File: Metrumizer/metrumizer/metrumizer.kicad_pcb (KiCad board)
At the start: 2 copper layers, 83 parts, among them J1 Conn_01x03, J2 USB_B_Micro, J3 Conn_01x04, J4 Conn_01x03, Q1 AO3401A, Q2 AO3401A, Q3 Si7232DN, U1 ATSAMD21G17A-M, U10 LM293, U2 CC1200, U3 W25Q128JVS, U4 ADXL375BCCZ-RL7, U5 MS5607-02BA, U6 MAX-M10S, U7 MCP130-315, U8 XC6206P332MR, Y1 X322516MLB4SI, Y2 YF4040M00033T8188097

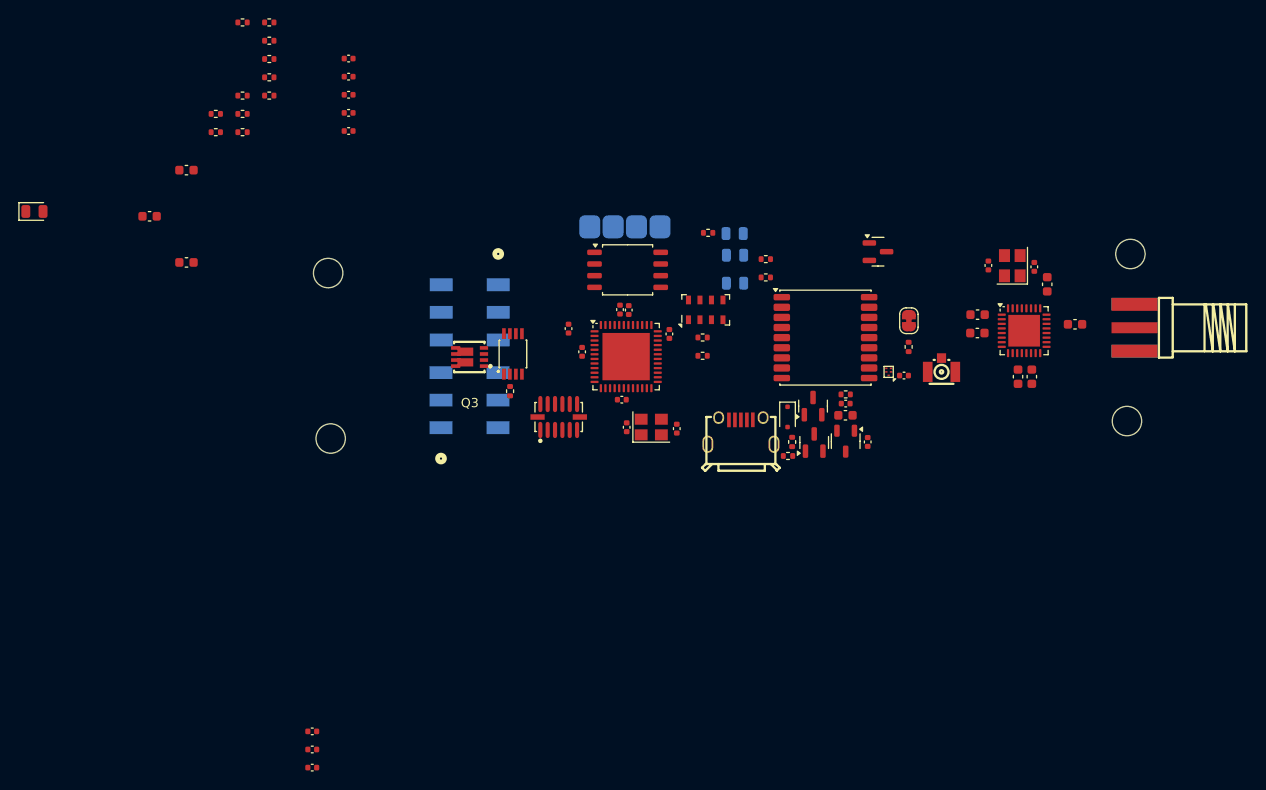
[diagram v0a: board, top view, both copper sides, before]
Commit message: dan f10, n511 module, board layout
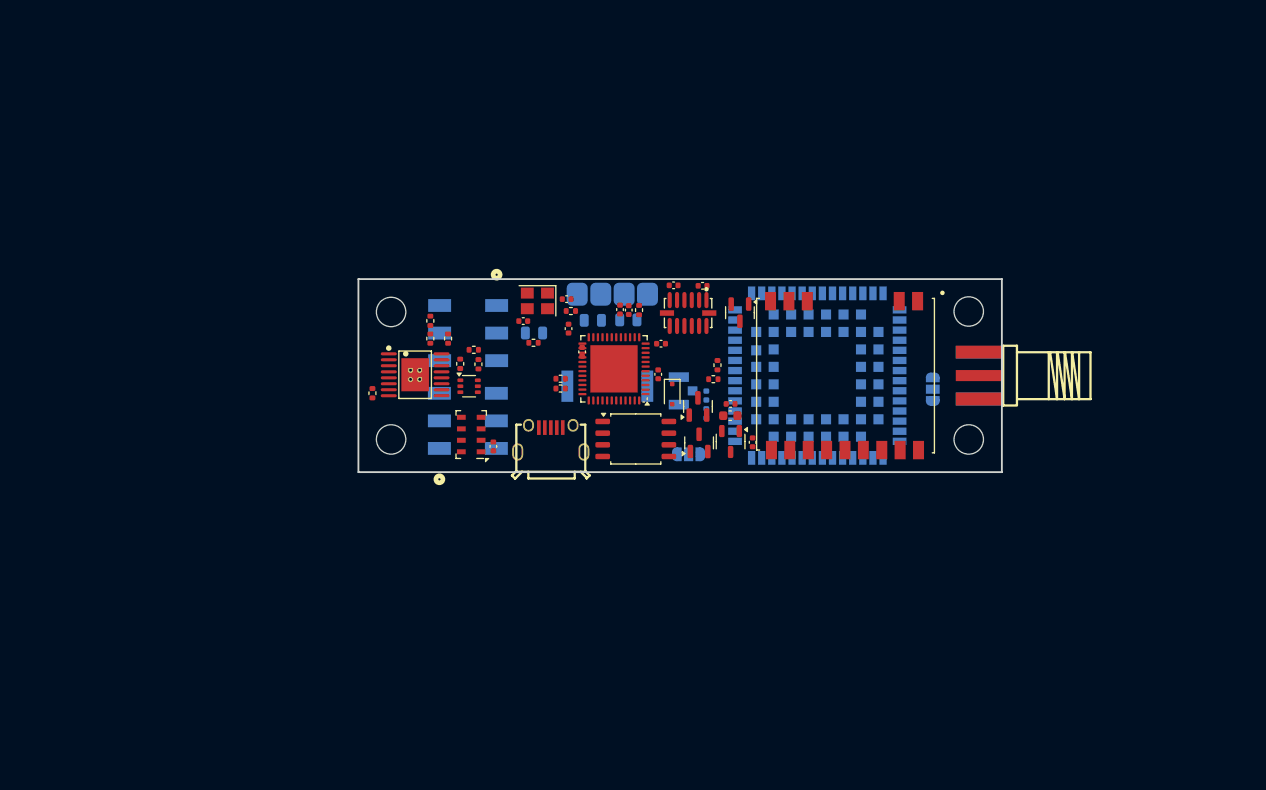
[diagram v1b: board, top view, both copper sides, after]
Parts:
- removed AE1: IPEX, .pretty:ANT-SMD_1909763-1
- removed C15, C19, C35: 10n, Capacitor_SMD:C_0402_1005Metric
- removed C16, C17: 20p, Capacitor_SMD:C_0402_1005Metric
- removed C18, C20, C21, C22, C24, C25, C26, C29: 47n, Capacitor_SMD:C_0603_1608Metric
- removed C23: 0.22u, Capacitor_SMD:C_0402_1005Metric
- removed C32: 2.2p, Capacitor_SMD:C_0402_1005Metric
- removed C34: 56p, Capacitor_SMD:C_0603_1608Metric
- removed C36: 100p, Capacitor_SMD:C_0402_1005Metric
- removed D5: LED, LED_SMD:LED_0805_2012Metric
- removed FL1: B39162B8813P810, Filter:Filter_1109-5_1.1x0.9mm
- removed JP1: jumper, Jumper:SolderJumper-2_P1.3mm_Bridged_RoundedPad1.0x1.5mm
- removed Q3: Si7232DN, .pretty:POWER-1212-8_L3.3-W3.3-P0.66-LS3.3-BL
- removed R10: 10, Resistor_SMD:R_0402_1005Metric
- removed R11, R13: 10k, Resistor_SMD:R_0402_1005Metric
- removed R21: 100k, Resistor_SMD:R_0402_1005Metric
- removed R22: 27k, Resistor_SMD:R_0402_1005Metric
- removed R6: 1k, Resistor_SMD:R_0402_1005Metric
- removed R7: 56k, Resistor_SMD:R_0402_1005Metric
- removed U2: CC1200, Package_DFN_QFN:QFN-32-1EP_5x5mm_P0.5mm_EP3.45x3.45mm
- removed U6: MAX-M10S, RF_GPS:ublox_MAX
- removed Y2: YF4040M00033T8188097, Crystal:Crystal_SMD_3225-4Pin_3.2x2.5mm
- added AE2: SMA, .pretty:CONN-SMD_KH-SMA-KE8-G, F.Cu at (198.7, 101.1)
- added BZ1: Buzzer, SamacSys_Parts:PKMCS0909E4000R1, B.Cu at (158.3, 102.2)
- added IC1: DAN-F10N-00B, KiCad:DANF10N00B, B.Cu at (181.1, 101.1)
- added JP2: SolderJumper_3_Open, Jumper:SolderJumper-3_P1.3mm_Open_RoundedPad1.0x1.5mm, B.Cu at (193.7, 102.5)
- added JP3: SolderJumper_3_Open, Jumper:SolderJumper-3_P1.3mm_Open_RoundedPad1.0x1.5mm, B.Cu at (167.1, 109.6)
- added L2: 27n, Inductor_SMD:L_0402_1005Metric, B.Cu at (169.1, 103.2)
- added R25: 1k, Resistor_SMD:R_0402_1005Metric, F.Cu at (132.7, 103.0)
- added U11: N511_433, .pretty:N511 433, F.Cu at (184.0, 101.1)
- added U9: TPS2H160BQPWPRQ1, .pretty:HTSSOP-16_L5.0-W4.4-P0.65-LS6.4-BL-EP-A, F.Cu at (137.4, 101.0)
- AE3: value SMA -> IPEX; footprint .pretty:CONN-SMD_KH-SMA-KE8-G -> .pretty:ANT-SMD_1909763-1; moved to B.Cu
- H1, H2, H3, H4: moved to B.Cu
- R15: value 1k -> 100k
- R16: value 3.3k -> 27k
- R17: value 3.3k -> 100k
- R18: value 1k -> 27k
- R20: value 27k -> 100k
- R8: value 56k -> 10; moved to B.Cu
- U10: value LM293 -> 74LVC2G14; footprint .pretty:MINISO-8_L3.0-W3.0-P0.65-LS4.9-BL -> Package_TO_SOT_SMD:SOT-363_SC-70-6
- moved R8 66.0 mm to (169.1, 105.2), turned to -90 degrees
- moved C13 65.9 mm to (168.7, 91.3), turned to 180 degrees
- moved C12 62.4 mm to (165.5, 91.2)
- moved AE3 49.3 mm to (166.8, 102.7), turned to 90 degrees
- moved R19 40.8 mm to (142.3, 99.8), turned to -90 degrees
- moved C14 40.1 mm to (145.9, 108.8), turned to 90 degrees
- moved R15 38.9 mm to (144.3, 99.8), turned to 90 degrees
- moved R18 36.9 mm to (139.0, 95.1), turned to -90 degrees
- moved R20 36.1 mm to (141.0, 97.0), turned to -90 degrees
- moved R16 35.9 mm to (143.8, 98.2)
- moved R17 30.4 mm to (139.0, 97.0), turned to 90 degrees
- moved U5 28.9 mm to (143.5, 107.5), turned to 180 degrees
- moved D1 24.4 mm to (150.3, 96.4)
- moved R1 22.4 mm to (150.3, 97.5), turned to 0 degrees
- moved R5 21.5 mm to (154.3, 94.0)
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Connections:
- J1 pad 3: /BATT POSTSW -> GND
- J1 pad 4: /BATT POSTSW -> GND
- J4 pad 1: /BATT POSTSW -> GND
- J4 pad 2: /BATT POSTSW -> GND
- R15 pad 1: /fire_a -> Net-(R15-Pad1)
- R15 pad 2: Net-(Q3-Pad4) -> /sense_a
- R16 pad 1: /fire_a -> GND
- R16 pad 2: GND -> /sense_a
- R17 pad 1: /fire_b -> Net-(R17-Pad1)
- R17 pad 2: GND -> /sense_b
- R18 pad 1: /fire_b -> GND
- R18 pad 2: Net-(Q3B-G2) -> /sense_b
- R19 pad 1: /fet_a -> +BATT
- R19 pad 2: /sense_a -> /fet_a
- R20 pad 1: GND -> +BATT
- R20 pad 2: /sense_a -> /fet_b
- R8 pad 2: GND -> /VCC_RF
- U10 pad 1: Net-(Q3B-G2) -> /fet_a
- U10 pad 2: /cmp_rail -> GND
- U10 pad 3: /cmp_ldo_in -> /fet_b
- U10 pad 4: GND -> Net-(R17-Pad1)
- U10 pad 5: /cmp_ldo_in -> +BATT
- U10 pad 6: /cmp_rail -> Net-(R15-Pad1)
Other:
- board outline added: 70 x 21 mm

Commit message: saves
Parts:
- moved J4 0.47 mm to (142.9, 96.4), turned to 90 degrees
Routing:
- added copper zone on In2.Cu, net +3V3
- added copper zone on In1.Cu, net GND
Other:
- copper layers 2 -> 4
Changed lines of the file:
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@@
 	(layers
 		(0 "F.Cu" signal)
+		(4 "In1.Cu" signal)
+		(6 "In2.Cu" signal)
 		(2 "B.Cu" signal)
 		(9 "F.Adhes" user "F.Adhesive")
@@
 	)
 	(setup
+		(stackup
+			(layer "F.SilkS"
+				(type "Top Silk Screen")
+			)
+			(layer "F.Paste"
+				(type "Top Solder Paste")
+			)
+			(layer "F.Mask"
+				(type "Top Solder Mask")
+				(thickness 0.01)
+			)
+			(layer "F.Cu"
+				(type "copper")
+				(thickness 0.035)
+			)
+			(layer "dielectric 1"
+				(type "prepreg")
+				(thickness 0.1)
+				(material "FR4")
+				(epsilon_r 4.5)
+				(loss_tangent 0.02)
+			)
+			(layer "In1.Cu"
+				(type "copper")
+				(thickness 0.035)
+			)
+			(layer "dielectric 2"
+				(type "core")
+				(thickness 1.24)
+				(material "FR4")
+				(epsilon_r 4.5)
+				(loss_tangent 0.02)
+			)
+			(layer "In2.Cu"
+				(type "copper")
+				(thickness 0.035)
+			)
+			(layer "dielectric 3"
+				(type "prepreg")
+				(thickness 0.1)
+				(material "FR4")
+				(epsilon_r 4.5)
+				(loss_tangent 0.02)
+			)
+			(layer "B.Cu"
+				(type "copper")
+				(thickness 0.035)
+			)
+			(layer "B.Mask"
+				(type "Bottom Solder Mask")
+				(thickness 0.01)
+			)
+			(layer "B.Paste"
+				(type "Bottom Solder Paste")
+			)
+			(layer "B.SilkS"
+				(type "Bottom Silk Screen")
+			)
+			(copper_finish "None")
+			(dielectric_constraints yes)
+		)
 		(pad_to_mask_clearance 0)
 		(allow_soldermask_bridges_in_footprints no)
@@
 		(model "C:/Users/E/Documents/GitHub/Lyra-flight-computer/Hardware/kicad/libs/easyeda2kicad/.3dshapes/ANT-TH_L13.5-W6.5-H6.5.wrl"
 			(offset
-				(xyz -0 5.43 2.8)
+				(xyz 0 2.93 0.5)
 			)
 			(scale
@@
 			)
 			(rotate
-				(xyz 0 0 270)
+				(xyz -0 -0 -90)
 			)
 		)
@@
 	(footprint "footprints:CONN3_2059-303&slash_998-403_WAG"
 		(layer "B.Cu")
-		(at 143.401301 96.431502 -90)
+		(at 142.929901 96.420102 90)
 		(tags "2059-303/998-403 ")
 		(property "Reference" "J4"
-			(at 0 0.249999 90)
+			(at 0 0.249999 270)
 			(unlocked yes)
 			(layer "B.SilkS")
@@
 		)
 		(property "Value" "Conn_01x03"
-			(at 0 0.249999 90)
+			(at 0 0.249999 270)
 			(unlocked yes)
 			(layer "B.Fab")
@@
 		)
 		(property "Datasheet" "~"
-			(at 0 0 90)
+			(at 0 0 270)
 			(unlocked yes)
 			(layer "B.Fab")
@@
 		)
 		(property "Description" "Generic connector, single row, 01x03, script generated (kicad-library-utils/schlib/autogen/connector/)"
-			(at 0 0 90)
+			(at 0 0 270)
 			(unlocked yes)
 			(layer "B.Fab")
@@
 		)
 		(property "Part #" "2059-323/998-403"
-			(at 0 0 90)
+			(at 0 0 270)
 			(unlocked yes)
 			(layer "B.Fab")
@@
 		)
 		(fp_line
-			(start -4.577 3.827)
-			(end -4.031238 3.827)
+			(start 4.577003 -3.827)
+			(end 4.03124 -3.827)
 			(stroke
 				(width 0.1524)
@@
 		)
 		(fp_line
-			(start -1.968758 3.827)
-			(end -1.031239 3.827)
+			(start 1.96876 -3.827)
+			(end 1.031241 -3.827)
 			(stroke
 				(width 0.1524)
@@
 		)
 		(fp_line
-			(start 1.031241 3.827)
-			(end 1.96876 3.827)
+			(start -1.031239 -3.827)
+			(end -1.968758 -3.827)
 			(stroke
 				(width 0.1524)
@@
 		)
 		(fp_line
-			(start 4.03124 3.827)
-			(end 4.577003 3.827)
+			(start -4.031238 -3.827)
+			(end -4.577 -3.827)
 			(stroke
 				(width 0.1524)
@@
 		)
 		(fp_line
-			(start 4.577003 3.827)
-			(end 4.577003 -3.827)
+			(start -4.577 -3.827)
+			(end -4.577 3.827)
 			(stroke
 				(width 0.1524)
@@
 		)
 		(fp_line
-			(start -4.577 -3.827)
-			(end -4.577 3.827)
+			(start 4.577003 3.827)
+			(end 4.577003 -3.827)
 			(stroke
 				(width 0.1524)
@@
 		)
 		(fp_line
-			(start -4.031238 -3.827)
-			(end -4.577 -3.827)
+			(start 4.03124 3.827)
+			(end 4.577003 3.827)
 			(stroke
 				(width 0.1524)
@@
 		)
 		(fp_line
-			(start -1.031239 -3.827)
-			(end -1.968758 -3.827)
+			(start 1.031241 3.827)
+			(end 1.96876 3.827)
 			(stroke
 				(width 0.1524)
@@
 		)
 		(fp_line
-			(start 1.96876 -3.827)
-			(end 1.031241 -3.827)
+			(start -1.968758 3.827)
+			(end -1.031239 3.827)
 			(stroke
 				(width 0.1524)
@@
 		)
 		(fp_line
-			(start 4.577003 -3.827)
-			(end 4.03124 -3.827)
+			(start -4.577 3.827)
+			(end -4.031238 3.827)
 			(stroke
 				(width 0.1524)
@@
 		)
 		(fp_line
-			(start -4.704 4.853998)
-			(end 4.704003 4.853998)
+			(start 4.704003 -4.353999)
+			(end -4.704 -4.353999)
 			(stroke
 				(width 0.1524)
@@
 		)
 		(fp_line
-			(start 4.704003 4.853998)
-			(end 4.704003 -4.353999)
+			(start -4.704 -4.353999)
+			(end -4.704 4.853998)
 			(stroke
 				(width 0.1524)
@@
 		)
 		(fp_line
-			(start -4.704 -4.353999)
-			(end -4.704 4.853998)
+			(start 4.704003 4.853998)
+			(end 4.704003 -4.353999)
 			(stroke
 				(width 0.1524)
@@
 		)
 		(fp_line
-			(start 4.704003 -4.353999)
-			(end -4.704 -4.353999)
+			(start -4.704 4.853998)
+			(end 4.704003 4.853998)
 			(stroke
 				(width 0.1524)
@@
 		)
 		(fp_line
-			(start -4.45 3.7)
-			(end 4.450003 3.7)
+			(start 4.450003 -3.7)
+			(end -4.45 -3.7)
 			(stroke
 				(width 0.0254)
@@
 		)
 		(fp_line
-			(start 4.450003 3.7)
-			(end 4.450003 -3.7)
+			(start -4.45 -3.7)
+			(end -4.45 3.7)
 			(stroke
 				(width 0.0254)
@@
 		)
 		(fp_line
-			(start -4.45 -3.7)
-			(end -4.45 3.7)
+			(start 4.450003 3.7)
+			(end 4.450003 -3.7)
 			(stroke
 				(width 0.0254)
@@
 		)
 		(fp_line
-			(start 4.450003 -3.7)
-			(end -4.45 -3.7)
+			(start -4.45 3.7)
+			(end 4.450003 3.7)
 			(stroke
 				(width 0.0254)
@@
 		)
 		(fp_text user "${REFERENCE}"
-			(at 0 0.249999 90)
+			(at 0 0.249999 270)
 			(unlocked yes)
 			(layer "B.Fab")
@@
 		)
 		(pad "1" smd rect
-			(at -2.999998 -2.849999 270)
+			(at -2.999998 -2.849999 90)
 			(size 1.397 2.5)
 			(layers "B.Cu" "B.Mask" "B.Paste")
@@
 		)
 		(pad "2" smd rect
-			(at -2.999998 3.349998 270)
+			(at -2.999998 3.349998 90)
 			(size 1.397 2.5)
 			(layers "B.Cu" "B.Mask" "B.Paste")
@@
 		)
 		(pad "3" smd rect
-			(at 0 -2.849999 270)
+			(at 0 -2.849999 90)
 			(size 1.397 2.5)
 			(layers "B.Cu" "B.Mask" "B.Paste")
@@
 		)
 		(pad "4" smd rect
-			(at 0 3.349998 270)
+			(at 0 3.349998 90)
 			(size 1.397 2.5)
 			(layers "B.Cu" "B.Mask" "B.Paste")
@@
 		)
 		(pad "5" smd rect
-			(at 3 -2.849999 270)
+			(at 3 -2.849999 90)
 			(size 1.397 2.5)
 			(layers "B.Cu" "B.Mask" "B.Paste")
@@
 		)
 		(pad "6" smd rect
-			(at 3 3.349998 270)
+			(at 3 3.349998 90)
 			(size 1.397 2.5)
 			(layers "B.Cu" "B.Mask" "B.Paste")
@@
 		(layer "Edge.Cuts")
 	)
+	(dimension
+		(type orthogonal)
+		(layer "Edge.Cuts")
+		(pts
+			(xy 131.2164 90.5568) (xy 201.2164 90.5568)
+		)
+		(height -11.4318)
+		(orientation 0)
+		(format
+			(prefix "")
+			(suffix "")
+			(units 0)
+			(units_format 1)
+			(precision 4)
+		)
+		(style
+			(thickness 0.05)
+			(arrow_length 1.27)
+			(text_position_mode 0)
+			(arrow_direction outward)
+			(extension_height 0.58642)
+			(extension_offset 0.5)
+			(keep_text_aligned yes)
+		)
+		(gr_text "2.7559 in"
+			(at 166.2164 77.975 0)
+			(layer "Edge.Cuts")
+			(effects
+				(font
+					(size 1 1)
+					(thickness 0.15)
+				)
+			)
+		)
+	)
+	(dimension
+		(type orthogonal)
+		(layer "Edge.Cuts")
+		(pts
+			(xy 131.2164 90.5568) (xy 131.2164 111.5568)
+		)
+		(height -20.4414)
+		(orientation 1)
+		(format
+			(prefix "")
+			(suffix "")
+			(units 0)
+			(units_format 1)
+			(precision 4)
+		)
+		(style
+			(thickness 0.05)
+			(arrow_length 1.27)
+			(text_position_mode 0)
+			(arrow_direction outward)
+			(extension_height 0.58642)
+			(extension_offset 0.5)
+			(keep_text_aligned yes)
+		)
+		(gr_text "0.8268 in"
+			(at 109.625 101.0568 90)
+			(layer "Edge.Cuts")
+			(effects
+				(font
+					(size 1 1)
+					(thickness 0.15)
+				)
+			)
+		)
+	)
+	(zone
+		(net 1)
+		(net_name "GND")
+		(layer "In1.Cu")
+		(hatch edge 0.5)
+		(connect_pads
+			(clearance 0.5)
+		)
+		(min_thickness 0.25)
+		(filled_areas_thickness no)
+		(fill yes
+			(thermal_gap 0.5)
+			(thermal_bridge_width 0.5)
+		)
+		(polygon
+			(pts
+				(xy 129 90.225) (xy 202.65 89.875) (xy 202.75 112.25) (xy 129.375 112.25)
+			)
+		)
+	)
+	(zone
+		(net 4)
+		(net_name "+3V3")
+		(layer "In2.Cu")
+		(hatch edge 0.5)
+		(connect_pads
+			(clearance 0.5)
+		)
+		(min_thickness 0.25)
+		(filled_areas_thickness no)
+		(fill yes
+			(thermal_gap 0.5)
+			(thermal_bridge_width 0.5)
+		)
+		(polygon
+			(pts
+				(xy 130.301446 90.354338) (xy 203.951446 90.004338) (xy 204.051446 112.379338) (xy 130.676446 112.379338)
+			)
+		)
+	)
 	(embedded_fonts no)

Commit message: weorjk
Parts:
- removed AE3: IPEX, .pretty:ANT-SMD_1909763-1
- removed H3, H4: MountingHole, MountingHole:MountingHole_3.2mm_M3
- removed IC1: DAN-F10N-00B, KiCad:DANF10N00B
- removed JP3: SolderJumper_3_Open, Jumper:SolderJumper-3_P1.3mm_Open_RoundedPad1.0x1.5mm
- removed L2: 27n, Inductor_SMD:L_0402_1005Metric
- removed R8: 10, Resistor_SMD:R_0402_1005Metric
- added AE1: IPEX, .pretty:ANT-SMD_1909763-1, F.Cu at (176.8, 106.7)
- added D5: LED, LED_SMD:LED_0805_2012Metric, B.Cu at (179.4, 105.4)
- added J5: Conn_01x02, Jumper:SolderJumper-2_P1.3mm_Open_Pad1.0x1.5mm, B.Cu at (178.6, 109.9)
- added L1: 27n, Inductor_SMD:L_0402_1005Metric, F.Cu at (175.3, 105.1)
- added R10: 10, Resistor_SMD:R_0402_1005Metric, F.Cu at (175.3, 103.2)
- added R6: 1k, Resistor_SMD:R_0402_1005Metric, F.Cu at (175.3, 96.8)
- added R7: 56k, Resistor_SMD:R_0402_1005Metric, F.Cu at (162.9, 108.2)
- added U6: MAX-M10S, RF_GPS:ublox_MAX, F.Cu at (168.7, 102.3)
- AE2, U11: moved to B.Cu
- H1: moved to F.Cu
- J3: value Conn_01x04 -> Conn_01x02; footprint .pretty:4 pads 2.54mm spacign -> Jumper:SolderJumper-2_P1.3mm_Open_Pad1.0x1.5mm
- moved C2 56.2 mm to (118.9, 98.1), turned to 0 degrees
- moved R24 52.2 mm to (117.9, 96.5)
- moved R23 52.2 mm to (118.4, 95.0)
- moved C1 48.4 mm to (123.4, 101.3), turned to -90 degrees
- moved JP2 39.9 mm to (154.8, 93.6)
- moved U8 37.0 mm to (135.0, 103.7), turned to 180 degrees
- moved D2 36.7 mm to (128.8, 105.9)
- moved Q2 34.4 mm to (134.9, 100.2), turned to 0 degrees
- moved C3 33.9 mm to (137.8, 103.6), turned to -90 degrees
- moved Q1 29.6 mm to (138.8, 100.1), turned to 0 degrees
- moved J3 28.2 mm to (178.6, 107.7)
- moved R2 26.8 mm to (127.9, 93.6)
- moved R3 26.8 mm to (127.9, 92.6)
- moved C11 23.3 mm to (127.5, 86.6)
- moved R1 23.3 mm to (128.6, 89.0)
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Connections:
- J3 pad 1: /reset_n -> /swclk
- J3 pad 2: /swdio -> GND
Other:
- board size 70 x 21 mm -> 50.8 x 20.3 mm

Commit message: cam control
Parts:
- removed Q2: AO3401A, Package_TO_SOT_SMD:SOT-23
- added C15: 100n, Capacitor_SMD:C_0402_1005Metric, F.Cu at (150.7, 110.2)
- added C16: 1n, Capacitor_SMD:C_0402_1005Metric, F.Cu at (135.3, 98.5)
- added C17: 10n, Capacitor_SMD:C_0402_1005Metric, F.Cu at (132.0, 100.7)
- added Q3: AO3401A, Package_TO_SOT_SMD:SOT-23, F.Cu at (137.8, 101.7)
- added Q4: AO3401A, Package_TO_SOT_SMD:SOT-23, F.Cu at (135.0, 103.8)
- added R8: 1k, Resistor_SMD:R_0402_1005Metric, F.Cu at (132.6, 98.5)
- added R9: 1k, Resistor_SMD:R_0402_1005Metric, F.Cu at (136.8, 99.0)
- added U2: HX6571, .pretty:SOT-23-3_L2.9-W1.6-P1.90-LS2.8-BR, F.Cu at (134.1, 100.0)
- moved R1 39.2 mm to (161.8, 109.8), turned to 180 degrees
- moved D1 34.9 mm to (179.1, 98.1)
- moved J3 27.5 mm to (152.6, 98.9), turned to 90 degrees
- moved J5 25.9 mm to (155.2, 98.9), turned to 90 degrees
- moved R4 24.9 mm to (138.4, 104.4)
- moved R24 24.0 mm to (141.2, 102.0), turned to 90 degrees
- moved R23 23.0 mm to (140.3, 102.0)
- moved R17 22.9 mm to (145.9, 94.1), turned to -90 degrees
- moved R5 22.8 mm to (137.5, 104.4), turned to -90 degrees
- moved R18 21.8 mm to (145.9, 95.9), turned to 90 degrees
- moved C11 21.5 mm to (147.9, 93.3), turned to 90 degrees
- moved C4 21.1 mm to (154.3, 104.4), turned to -90 degrees
- moved R16 20.3 mm to (144.5, 92.8), turned to 90 degrees
- moved C1 20.0 mm to (143.3, 99.4)
- moved R3 19.6 mm to (144.9, 102.4)
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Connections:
- U3 pad 4: +3V3 -> GND
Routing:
- net +BATT: track 0.00 -> 18.4 mm
- net Net-(D2-K): track 0.00 -> 16.9 mm
- net /BATT POSTSW: track 0.00 -> 12.7 mm, vias 0 -> 1
- net VBUS: track 0.00 -> 11.9 mm
- net GND: track 0.00 -> 10.1 mm, vias 0 -> 35
- net Net-(AE2-A): track 0.00 -> 7.78 mm
- net /USB_D-: track 0.00 -> 5.54 mm
- net /ATSAM D+: track 0.00 -> 5.42 mm
- net /ATSAM D-: track 0.00 -> 5.18 mm
- net Net-(Q3-G): track 0.00 -> 4.87 mm, vias 0 -> 2
- net /USB_D+: track 0.00 -> 4.55 mm
- net /MAG LATCH: track 0.00 -> 4.17 mm
- net Net-(AE1-A): track 0.00 -> 3.72 mm
- net +3V3: track 0.00 -> 2.75 mm, vias 0 -> 1
- net /VCC_RF: track 0.00 -> 2.13 mm
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- added copper zone on B.Cu, net GND
- added copper zone on F.Cu, net GND
- added copper zone on In2.Cu, net GND

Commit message: things
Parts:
- removed R19, R20: 100k, Resistor_SMD:R_0402_1005Metric
- removed R25: 1k, Resistor_SMD:R_0402_1005Metric
- removed U10: 74LVC2G14, Package_TO_SOT_SMD:SOT-363_SC-70-6
- added C18: 1u, Capacitor_SMD:C_0402_1005Metric, F.Cu at (133.9, 92.4)
- added Q2: AO3400A, Package_TO_SOT_SMD:SOT-23, F.Cu at (135.0, 95.9)
- added Q5: AO3400A, Package_TO_SOT_SMD:SOT-23, F.Cu at (139.2, 93.4)
- added R11: 510, Resistor_SMD:R_0402_1005Metric, F.Cu at (135.4, 93.5)
- U9: value TPS2H160BQPWPRQ1 -> TPS25970LRPWR; footprint .pretty:HTSSOP-16_L5.0-W4.4-P0.65-LS6.4-BL-EP-A -> easyeda2kicad2:QFN-10-2x2-hotrod
- moved U9 4.40 mm to (142.1, 96.2), turned to 0 degrees
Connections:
- net /BATT POSTSW renamed /BATT PRESW
- J1 pad 3: GND -> /PYRO PWR
- J1 pad 4: GND -> /PYRO PWR
- J4 pad 1: GND -> /PYRO PWR
- J4 pad 2: GND -> /PYRO PWR
- R15 pad 1: Net-(R15-Pad1) -> /fet_a
- R17 pad 1: Net-(R17-Pad1) -> /fet_b
- U9 pad 1: /fire_b -> /PWRB EN
- U9 pad 2: /fire_a -> GND
- U9 pad 5: unconnected-(U9-SEL-Pad5) -> +BATT
- U9 pad 6: unconnected-(U9-CS-Pad6) -> /PYRO PWR
- U9 pad 7: Net-(U9-CL) -> unconnected-(U9-DVDT-Pad7)
- U9 pad 9: GND -> Net-(U9-ILM)
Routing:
- net +BATT: track 18.4 -> 0.00 mm
- net Net-(D2-K): track 16.9 -> 0.00 mm
- net /BATT PRESW: track 12.7 -> 0.00 mm, vias 1 -> 0
- net VBUS: track 11.9 -> 0.00 mm
- net GND: track 10.1 -> 0.00 mm, vias 35 -> 24
- net /USB_D-: track 5.54 -> 0.00 mm
- net /ATSAM D+: track 5.42 -> 0.00 mm
- net /ATSAM D-: track 5.18 -> 0.00 mm
- net Net-(Q3-G): track 4.87 -> 0.00 mm, vias 2 -> 0
- net /USB_D+: track 4.55 -> 0.00 mm
- net /MAG LATCH: track 4.17 -> 0.00 mm
- net +3V3: track 2.75 -> 0.00 mm, vias 1 -> 0
- net Net-(Q3-D): track 1.55 -> 0.00 mm
- net /v_batt: track 0.95 -> 0.00 mm
